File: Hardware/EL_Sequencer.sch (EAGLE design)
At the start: 106 parts, among them J1 Battery, J2 DC-OUTPUT, J3 AC-INPUT, U1 LM317, U10 Z0103MN, U11 Z0103MN, U12 Z0103MN, U13 MOC3063S, U14 MOC3063S, U15 MOC3063S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

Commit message: Version 2.1 hardware files
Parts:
- added U$9: REVISION, SparkFun-Aesthetics:REVISION
- C1, C4, C5, C6, C7: device SparkFun:CAP0402-CAP -> SparkFun-Capacitors:0.1UF-25V(+80/-20%)(0603)
- C2, C3: device SparkFun:CAP_POL1206 -> SparkFun-Capacitors:10UF-16V-10%(TANT)
- R1: device SparkFun:RESISTOR0603-RES -> SparkFun-Resistors:390OHM1/10W1%(0603)
- R10, R11, R12, R13, R22, R23, R24, R25: device SparkFun:RESISTOR0402-RES -> SparkFun-Resistors:390OHM1/10W1%(0603)
- R14, R15, R16, R17, R18, R19, R20, R21, R26, R27, R28, R29, R30, R31, R32, R33: device SparkFun:RESISTOR0603-RES -> SparkFun-Resistors:330OHM1/10W1%(0603)
- R2: device SparkFun:RESISTOR0603-RES -> SparkFun-Resistors:240OHM1/10W1%(0603)
- R3, R5, R7, R9: device SparkFun:RESISTOR0402-RES -> SparkFun-Resistors:1KOHM1/10W1%(0603)
- R4, R6: device SparkFun:RESISTOR0402-RES -> SparkFun-Resistors:2.0KOHM1/10W5%(0603)
- R8: device SparkFun:RESISTOR0402-RES -> SparkFun-Resistors:10KOHM1/10W1%(0603)0603
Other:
- note added: "ARDUINO PINS"
- note added: "T. Klopfenstein"
- note removed: "ARDUINO"
- note removed: "PINS"

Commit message: Fixing versions to 2.2
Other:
- note added: "2.2"
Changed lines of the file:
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@@
 <text x="205.74" y="93.98" size="1.778" layer="94">D13</text>
 <text x="166.116" y="11.176" size="2.54" layer="94">N. Seidle, M. Grusin</text>
-<text x="238.76" y="7.62" size="2.54" layer="94">2.1</text>
+<text x="238.76" y="7.62" size="2.54" layer="94">2.2</text>
 <text x="10.16" y="58.42" size="1.778" layer="97">Short SJ1 to bypass regulator</text>
 <text x="10.16" y="60.96" size="1.778" layer="97">3.3V regulator for external inverter</text>

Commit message: changed fiducials
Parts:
- removed U$3, U$4: FIDUCIALUFIDUCIAL, SparkFun-Aesthetics:FIDUCIALUFIDUCIAL
- added FID1, FID2: FIDUCIAL1X2, SparkFun-Aesthetics:FIDUCIAL1X2
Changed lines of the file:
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@@
 <part name="JP6" library="SparkFun" deviceset="M02" device="PTH"/>
 <part name="JP1" library="SparkFun" deviceset="M02" device="PTH"/>
-<part name="U$3" library="SparkFun-Aesthetics" deviceset="FIDUCIAL" device="UFIDUCIAL"/>
-<part name="U$4" library="SparkFun-Aesthetics" deviceset="FIDUCIAL" device="UFIDUCIAL"/>
 <part name="GND21" library="SparkFun" deviceset="GND" device=""/>
 <part name="Y1" library="SparkFun" deviceset="RESONATOR" device="SMD" value="8MHz"/>
@@
 <part name="FRAME1" library="SparkFun-Aesthetics" deviceset="FRAME-LETTER" device=""/>
 <part name="FRAME2" library="SparkFun-Aesthetics" deviceset="FRAME-LETTER" device=""/>
+<part name="FID1" library="SparkFun-Aesthetics" deviceset="FIDUCIAL" device="1X2"/>
+<part name="FID2" library="SparkFun-Aesthetics" deviceset="FIDUCIAL" device="1X2"/>
 </parts>
 <sheets>
@@
 <instance part="JP6" gate="G$1" x="93.98" y="48.26" rot="R180"/>
 <instance part="JP1" gate="G$1" x="12.7" y="134.62"/>
-<instance part="U$3" gate="G$1" x="241.3" y="27.94"/>
-<instance part="U$4" gate="G$1" x="241.3" y="25.4"/>
 <instance part="GND21" gate="1" x="142.24" y="119.38"/>
 <instance part="Y1" gate="G$1" x="152.4" y="124.46" rot="R270"/>
@@
 <instance part="FRAME1" gate="G$1" x="0" y="0"/>
 <instance part="FRAME1" gate="G$2" x="147.32" y="0"/>
+<instance part="FID1" gate="G$1" x="241.3" y="27.94"/>
+<instance part="FID2" gate="G$1" x="241.3" y="30.48"/>
 </instances>
 <busses>

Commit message: Adding Schottky diode to 5VUSB line for feedback protection
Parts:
- added D1: PMEG4005EJ, SparkFun-DiscreteSemi:DIODE-SCHOTTKY-PMEG4005EJ
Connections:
- new net DIO_VBUS: D1.C, S1.3, S1.6
- net 5VUSB: now also D1.A; no longer S1.3, S1.6
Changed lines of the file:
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@@
 <layer number="106" name="bPlate" color="7" fill="1" visible="yes" active="yes"/>
 <layer number="107" name="Crop" color="7" fill="1" visible="yes" active="yes"/>
+<layer number="108" name="tplace-old" color="10" fill="1" visible="yes" active="yes"/>
+<layer number="109" name="ref-old" color="11" fill="1" visible="yes" active="yes"/>
 <layer number="116" name="Patch_BOT" color="9" fill="4" visible="yes" active="yes"/>
 <layer number="121" name="_tsilk" color="7" fill="1" visible="yes" active="yes"/>
@@
 <part name="FID1" library="SparkFun-Aesthetics" deviceset="FIDUCIAL" device="1X2"/>
 <part name="FID2" library="SparkFun-Aesthetics" deviceset="FIDUCIAL" device="1X2"/>
+<part name="D1" library="SparkFun-DiscreteSemi" deviceset="DIODE-SCHOTTKY" device="-PMEG4005EJ" value="PMEG4005EJ"/>
 </parts>
 <sheets>
@@
 <instance part="FID1" gate="G$1" x="241.3" y="27.94"/>
 <instance part="FID2" gate="G$1" x="241.3" y="30.48"/>
+<instance part="D1" gate="G$1" x="22.86" y="160.02"/>
 </instances>
 <busses>
@@
 </segment>
 <segment>
-<wire x1="38.1" y1="160.02" x2="25.4" y2="160.02" width="0.1524" layer="91"/>
+<pinref part="D1" gate="G$1" pin="A"/>
+<wire x1="20.32" y1="160.02" x2="15.24" y2="160.02" width="0.127" layer="91"/>
+<label x="15.24" y="160.02" size="1.27" layer="95" rot="R180" xref="yes"/>
+</segment>
+</net>
+<net name="DIO_VBUS" class="0">
+<segment>
 <wire x1="38.1" y1="160.02" x2="40.64" y2="160.02" width="0.1524" layer="91"/>
 <wire x1="38.1" y1="160.02" x2="38.1" y2="152.4" width="0.1524" layer="91"/>
 <wire x1="38.1" y1="152.4" x2="40.64" y2="152.4" width="0.1524" layer="91"/>
-<junction x="38.1" y="160.02"/>
 <pinref part="S1" gate="G$1" pin="6"/>
 <pinref part="S1" gate="G$1" pin="3"/>
-<label x="25.4" y="160.02" size="1.27" layer="95" rot="R180" xref="yes"/>
-</segment>
-</net>
+<pinref part="D1" gate="G$1" pin="C"/>
+<wire x1="25.4" y1="160.02" x2="38.1" y2="160.02" width="0.127" layer="91"/>
+</segment>
+</net>

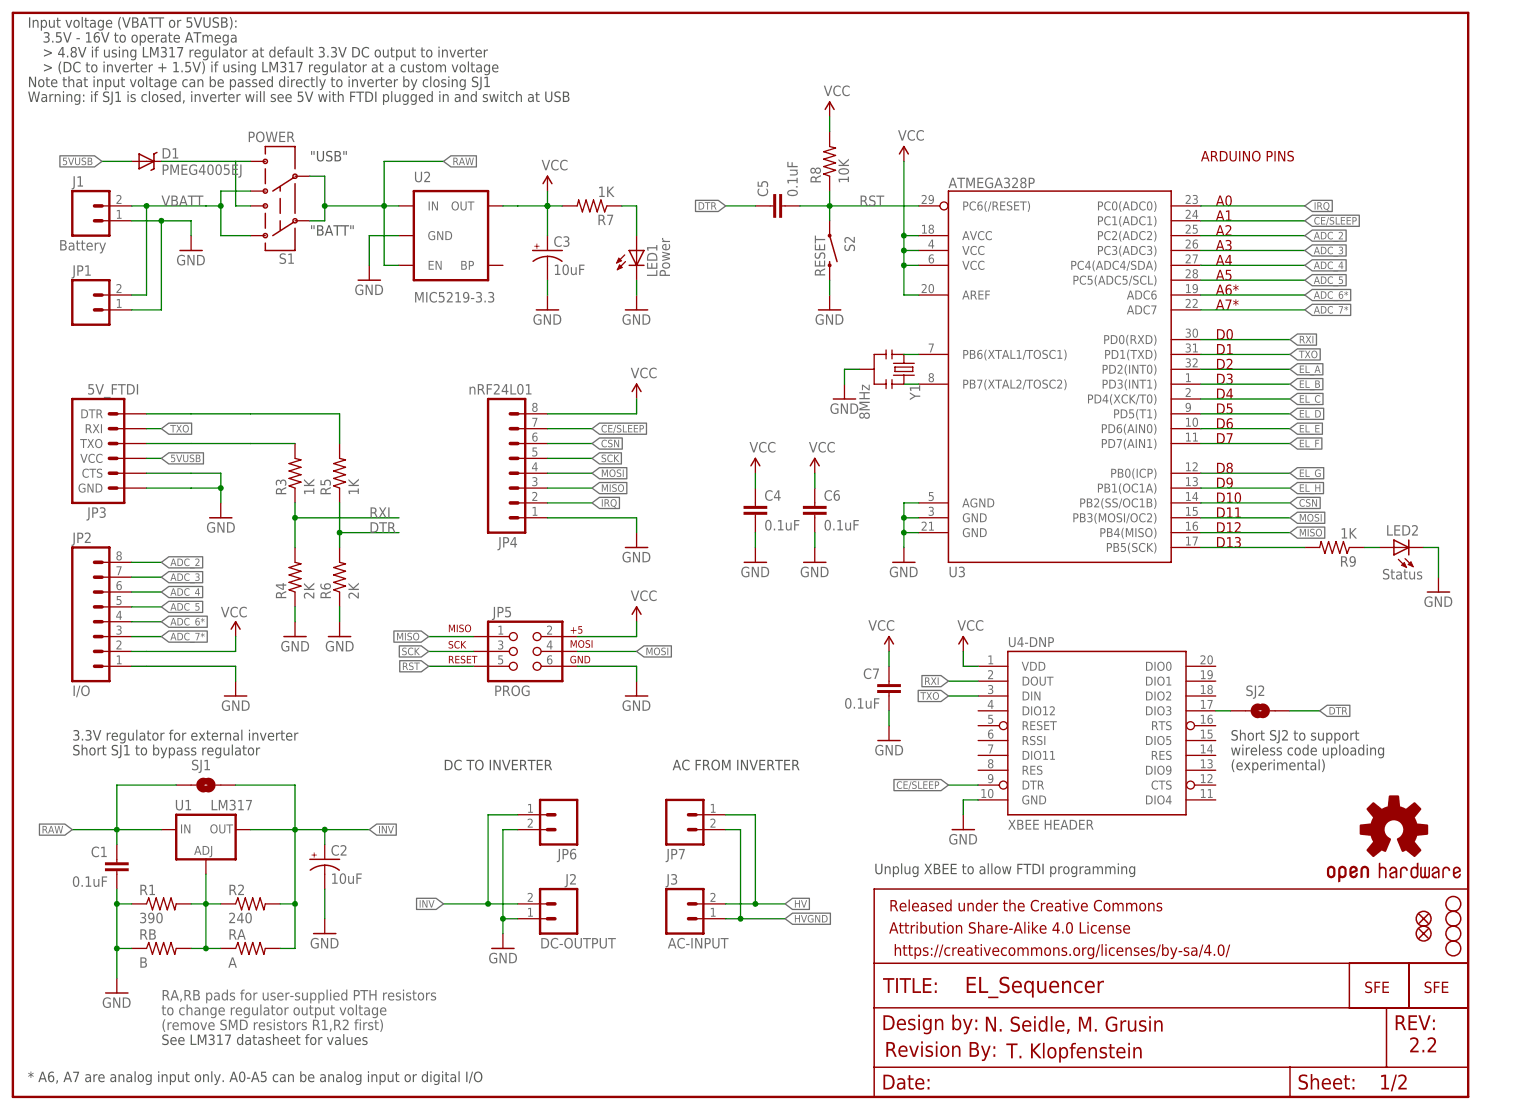
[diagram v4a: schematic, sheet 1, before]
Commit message: Adding in switch for FTDI/XBee selection
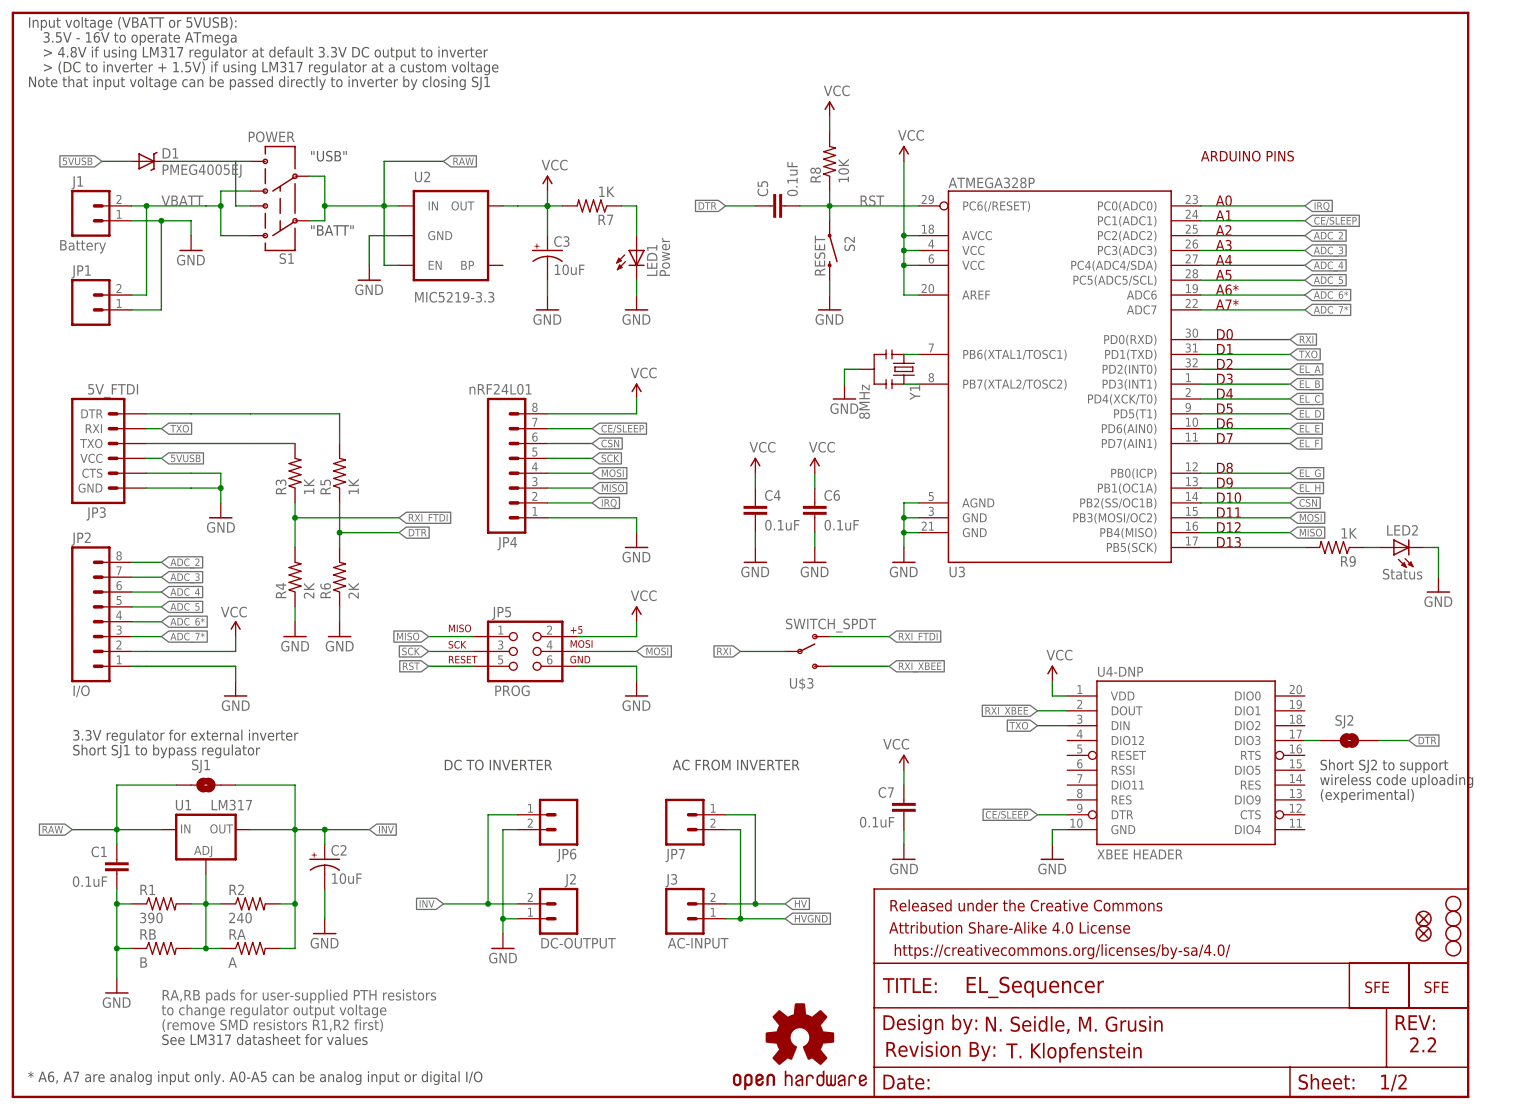
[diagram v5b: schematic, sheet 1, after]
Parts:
- added U$3: SWITCH_SPDT, SparkFun-Electromechanical:SWITCH_SPDT
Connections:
- new net RXI_FTDI: R3.1, R4.2, U$3.O
- new net RXI_XBEE: U$3.S, U4-DNP.DOUT
- net RXI: now also U$3.P; no longer R3.1, R4.2, U4-DNP.DOUT
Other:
- note removed: "Unplug XBEE to allow FTDI programming"
- note removed: "Warning: if SJ1 is closed, inverter will see 5V with FTDI plugged in and switch at USB"
- moved on the sheet: C7, SJ2, U4-DNP

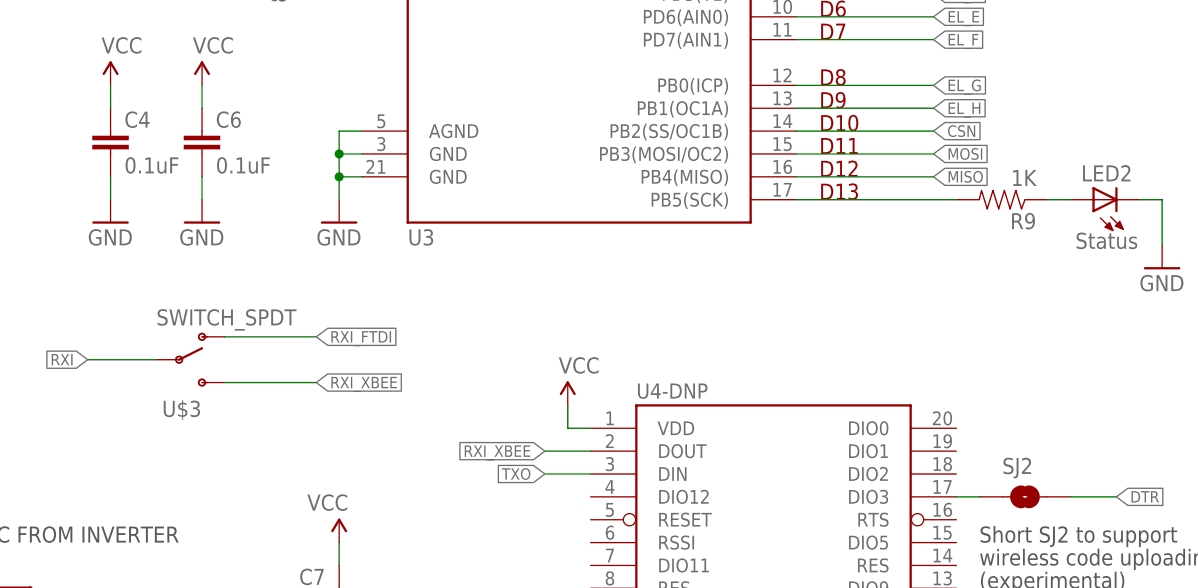
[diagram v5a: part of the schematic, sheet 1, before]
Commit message: Very minor adjustments
Fixed misaligned text in bplace (probably old)
Minor routing tweaks to switch pads (centered trc)
Renamed switch from U$3 to S3 (lib problem)
Reduced R9 to 470 to brighten green LED2
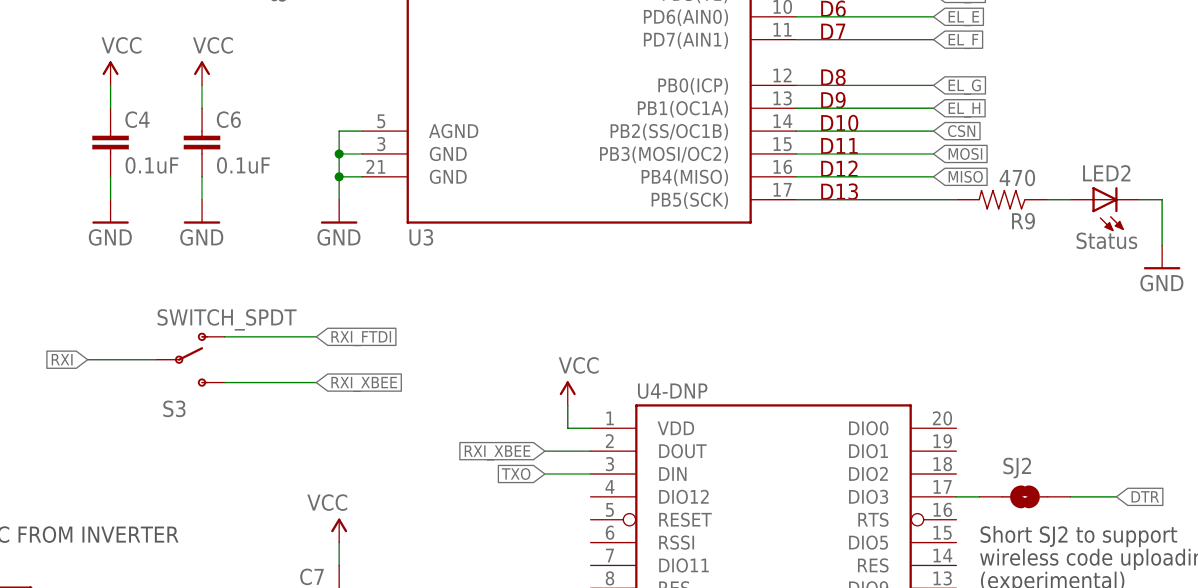
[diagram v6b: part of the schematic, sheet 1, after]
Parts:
- R9: value 1K -> 470
- renumbered U$3 to S3
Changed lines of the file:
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@@
 <?xml version="1.0" encoding="utf-8"?>
 <!DOCTYPE eagle SYSTEM "eagle.dtd">
-<eagle version="6.5.0">
+<eagle version="6.4">
 <drawing>
 <settings>
@@
 <part name="U3" library="SparkFun" deviceset="ATMEGA168" device="" value="ATMEGA328P"/>
 <part name="LED2" library="SparkFun" deviceset="LED" device="0603" value="Status"/>
-<part name="R9" library="SparkFun-Resistors" deviceset="1KOHM1/10W1%(0603)" device="" value="1K"/>
+<part name="R9" library="SparkFun-Resistors" deviceset="1KOHM1/10W1%(0603)" device="" value="470"/>
 <part name="GND14" library="SparkFun" deviceset="GND" device=""/>
 <part name="GND15" library="SparkFun" deviceset="GND" device=""/>
@@
 <part name="FID2" library="SparkFun-Aesthetics" deviceset="FIDUCIAL" device="1X2"/>
 <part name="D1" library="SparkFun-DiscreteSemi" deviceset="DIODE-SCHOTTKY" device="-PMEG4005EJ" value="PMEG4005EJ"/>
-<part name="U$3" library="SparkFun-Electromechanical" deviceset="SWITCH_SPDT" device=""/>
+<part name="S3" library="SparkFun-Electromechanical" deviceset="SWITCH_SPDT" device=""/>
 </parts>
 <sheets>
@@
 <instance part="FID2" gate="G$1" x="241.3" y="30.48"/>
 <instance part="D1" gate="G$1" x="22.86" y="160.02"/>
-<instance part="U$3" gate="G$1" x="134.62" y="76.2"/>
+<instance part="S3" gate="G$1" x="134.62" y="76.2"/>
 </instances>
 <busses>
@@
 </segment>
 <segment>
-<pinref part="U$3" gate="G$1" pin="P"/>
+<pinref part="S3" gate="G$1" pin="P"/>
 <wire x1="124.46" y1="76.2" x2="132.08" y2="76.2" width="0.2032" layer="91"/>
 <label x="124.46" y="76.2" size="1.27" layer="95" rot="R180" xref="yes"/>
@@
 <net name="RXI_FTDI" class="0">
 <segment>
-<pinref part="U$3" gate="G$1" pin="O"/>
+<pinref part="S3" gate="G$1" pin="O"/>
 <wire x1="139.7" y1="78.74" x2="149.86" y2="78.74" width="0.2032" layer="91"/>
 <label x="149.86" y="78.74" size="1.27" layer="95" xref="yes"/>
@@
 <net name="RXI_XBEE" class="0">
 <segment>
-<pinref part="U$3" gate="G$1" pin="S"/>
+<pinref part="S3" gate="G$1" pin="S"/>
 <wire x1="139.7" y1="73.66" x2="149.86" y2="73.66" width="0.2032" layer="91"/>
 <label x="149.86" y="73.66" size="1.27" layer="95" xref="yes"/>
